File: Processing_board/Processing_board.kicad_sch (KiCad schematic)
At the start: 30 parts, among them J1 Conn_01x08_Pin, J2 Conn_01x08_Pin, J3 Conn_01x06_Pin, J4 Conn_01x03_Pin, J5 Conn_01x03_Pin, J6 Conn_01x02_Pin, J7 Conn_01x02_Pin, SW1 TL3305BF100QG, SW2 TL3305BF100QG, U1 STM32WBA63CIU6

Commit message: UART3 doesn't exist, modified block diagram
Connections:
- net USART3_RX renamed GPIO_IN
- net GPIO_IN: now also U1.6 (PA7); no longer U1.9 (PA5)
- net USART3_RX_CONN renamed GPIO_IN_CONN
- net USART3_TX renamed GPIO_OUT
- net GPIO_OUT: now also U1.9 (PA5); no longer U1.6 (PA7)
- net USART3_TX_CONN renamed GPIO_OUT_CONN
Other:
- note added: "GPIO_Output"
- note removed: "USART3 RX"
- note removed: "USART3_TX"
- note removed: "USART_3"

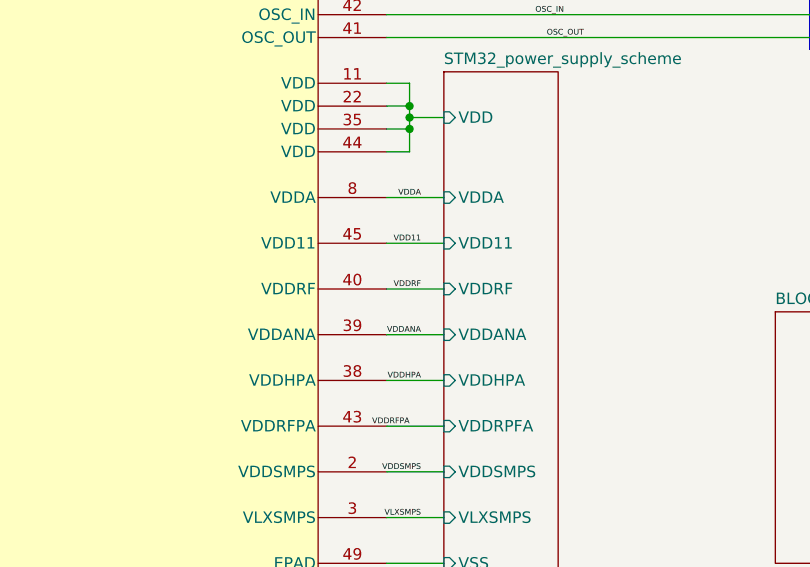
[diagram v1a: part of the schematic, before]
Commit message: connected VDDRF to 3V3, but errors still remaining
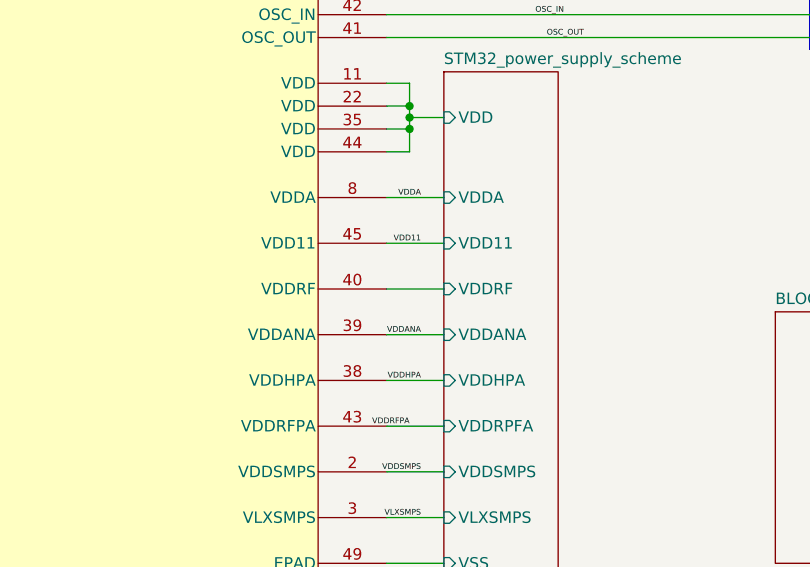
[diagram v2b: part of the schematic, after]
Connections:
- net VDDRF renamed STM32_power_supply_scheme/VDDRF

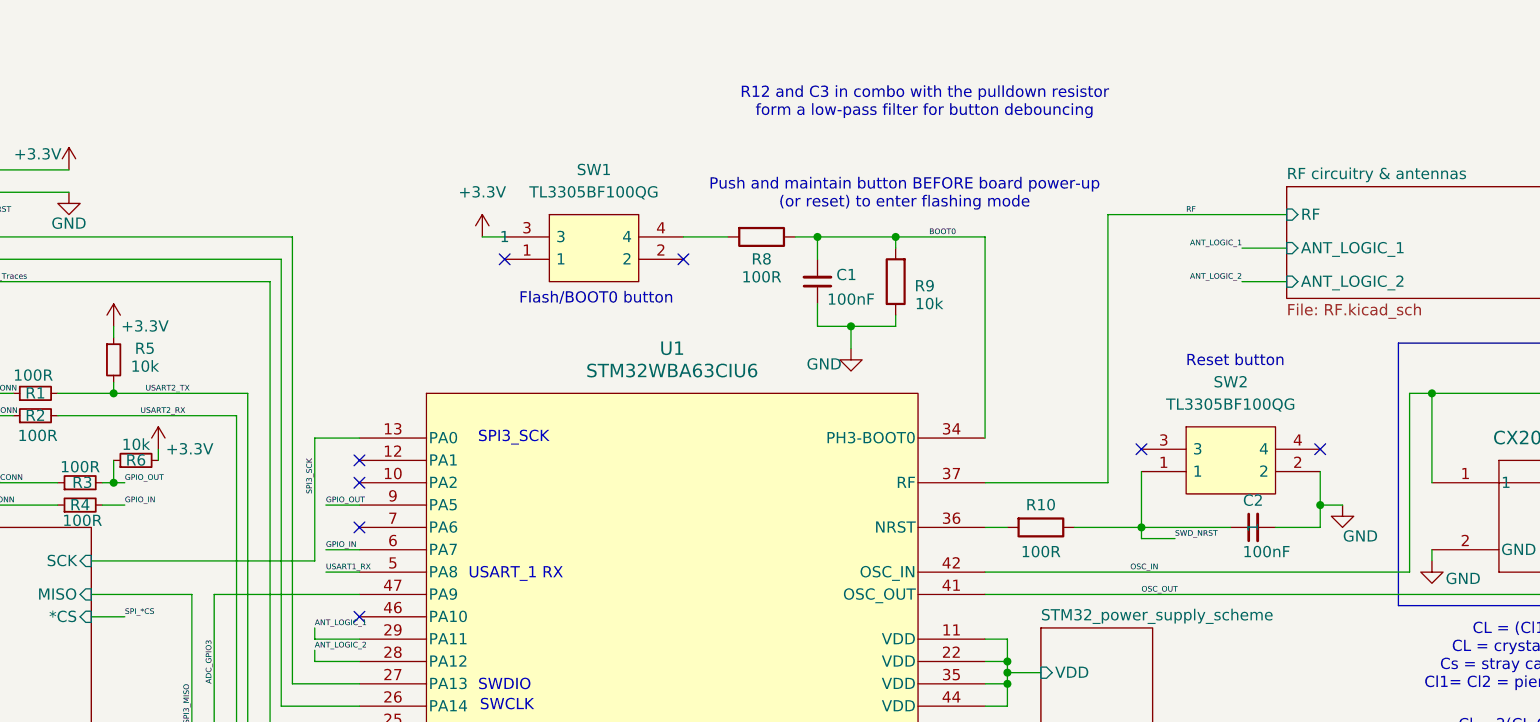
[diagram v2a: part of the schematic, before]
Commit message: rewired buttons BOOT and RESET correctly to avoid short circuit
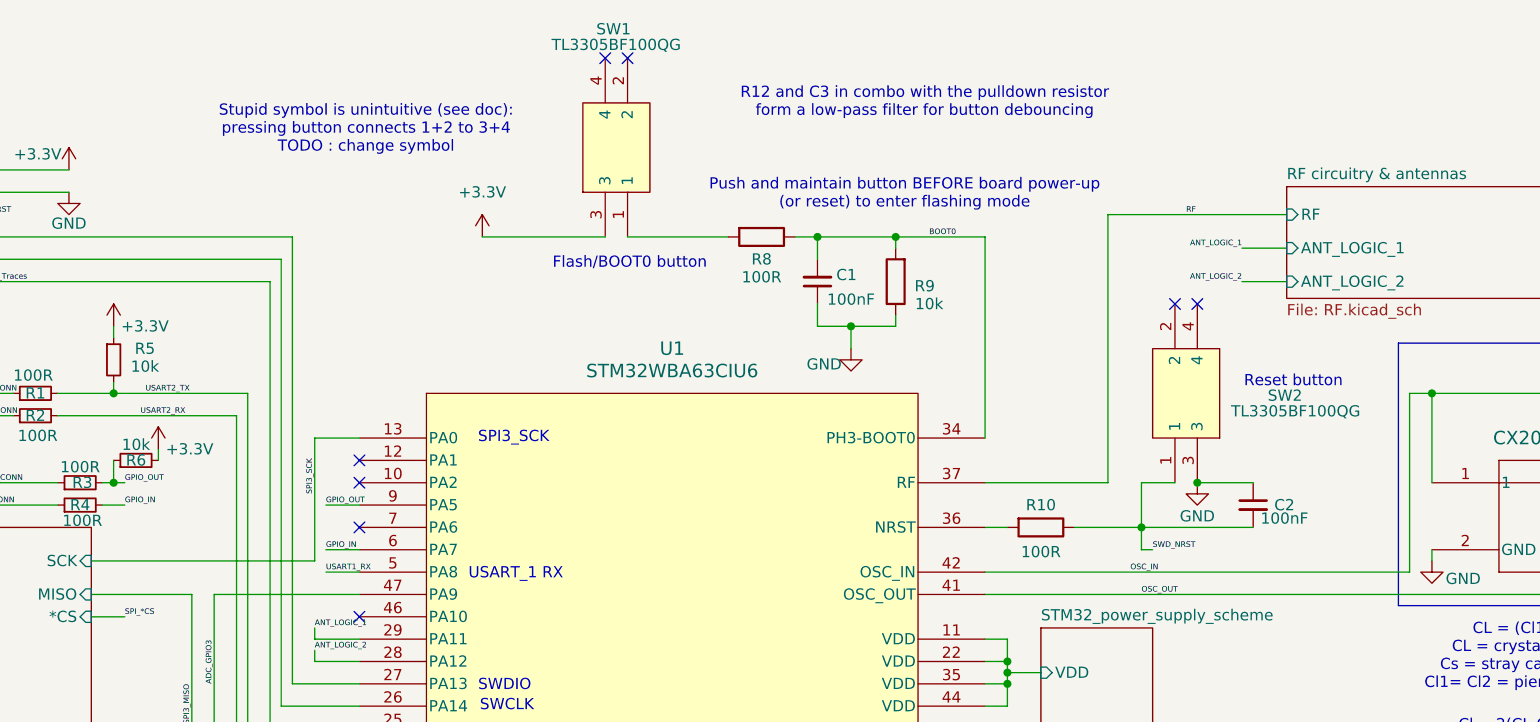
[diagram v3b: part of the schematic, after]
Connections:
- net GND: now also C2.1, SW2.3; no longer C2.2, SW2.2
- net SWD_NRST: now also C2.2; no longer C2.1
- net at R8.2: now also SW1.1; no longer SW1.4
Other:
- note added: "Stupid symbol is unintuitive (see doc): pressing button connects 1+2 to 3+4 TODO : change symbol"
- moved on the sheet: C2, SW1, SW2

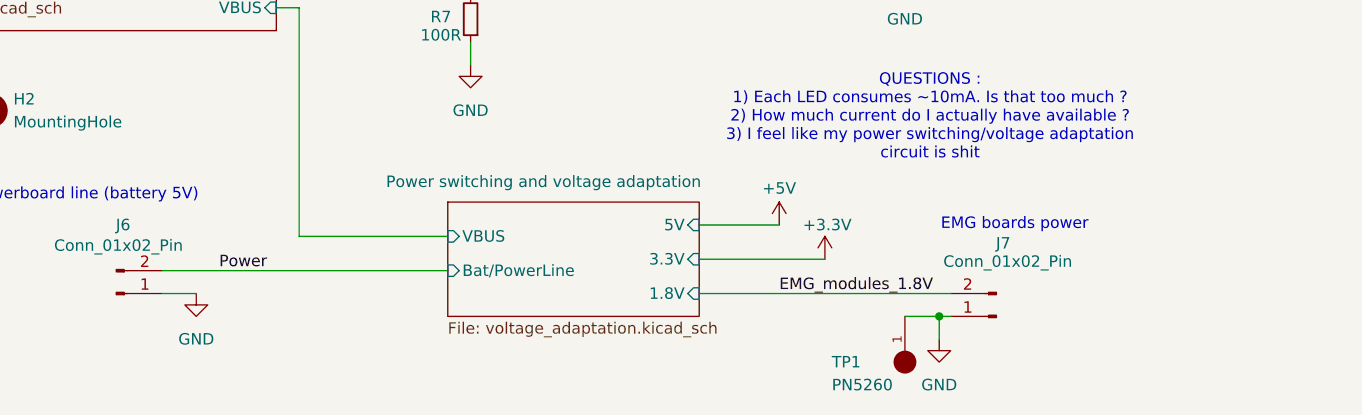
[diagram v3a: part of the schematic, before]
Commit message: feat: connected GNDA, VDDA, active electrodes and REF.
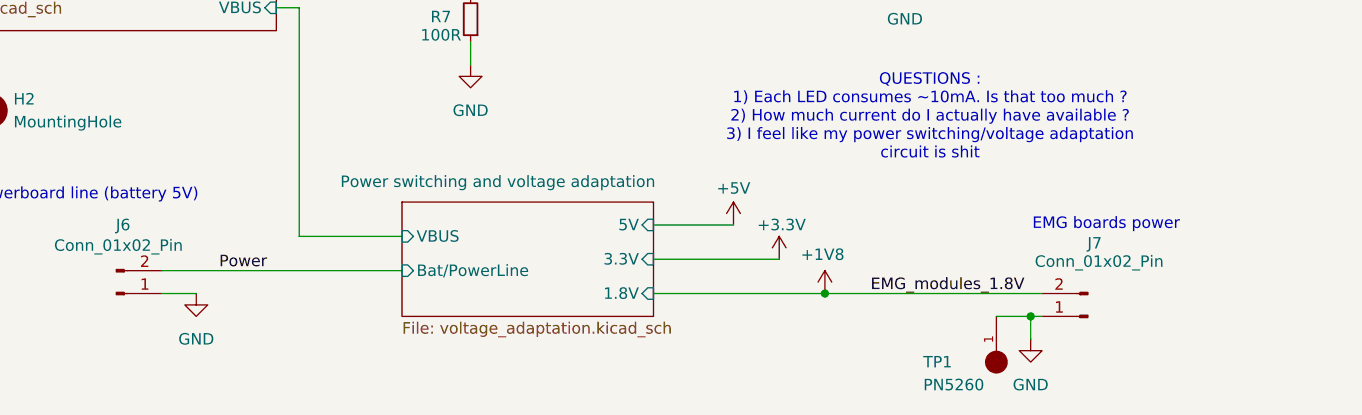
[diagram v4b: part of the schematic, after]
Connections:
- net EMG_modules_1.8V renamed +1V8
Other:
- moved on the sheet: J7, TP1
